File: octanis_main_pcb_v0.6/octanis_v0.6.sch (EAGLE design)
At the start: 103 parts, among them IC1 BME280, IC2 BNO055A, Q1 32.768kHz, Q2 32.768kHz, U1 TPS61232, U10 INA210, U11 INA210, U12 INA210, U13 RN2483, U2 DRV8836DSSR, U3 DRV8836DSSR, U4 MSP432, U5 SST25VF064C, U6 DRV8836DSSR, U7 DRV8836DSSR, U8 MAX6001SOT-23, U9 INA210

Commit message: finalized changes for v0.6. coax connector missing
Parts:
- added DIGITAL_IO2: (no value), pinhead:PINHD-2X5
- added JP1: (no value), pinhead:PINHD-2X2
- added V_MOT1, V_MOT2: (no value), pinhead-2:PINHD-1X02_2.54-S
- added X1: MC-921, con-coax:MC-921
- ANALOG: device pinhead:PINHD-2X10 -> pinhead:PINHD-2X5
- renumbered DIGITAL_IO to DIGITAL_IO1, M7/M1 to M7/M8
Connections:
- removed net A0: ANALOG.1
- removed net P3.7: DIGITAL_IO1.6, U4.P3.7/PM_UCB2SOMI/PM_UCB2SCL
- removed net P5.6_NC: U4.P5.6/TA2.1/VREF+/VEREF+/C1.7
- new net P10.4: DIGITAL_IO2.6, U4.P10.4/TA3.0/C0.7
- new net P10.5: DIGITAL_IO2.5, U4.P10.5/TA3.1/C0.6
- new net P2.1: DIGITAL_IO2.8, U4.P2.1/PM_UCA1CLK
- new net P2.4: DIGITAL_IO2.2, U4.P2.4/PM_TA0.1
- new net P2.5: DIGITAL_IO2.1, U4.P2.5/PM_TA0.2
- new net P2.6: DIGITAL_IO2.4, U4.P2.6/PM_TA0.3
- new net P2.7: DIGITAL_IO2.3, U4.P2.7/PM_TA0.4
- new net P5.6: DIGITAL_IO1.6, U4.P5.6/TA2.1/VREF+/VEREF+/C1.7
- new net P7.4: DIGITAL_IO2.7, U4.P7.4/PM_TA1.4/C0.5
- new net P7.5: DIGITAL_IO2.10, U4.P7.5/PM_TA1.3/C0.4
- new net P7.6: DIGITAL_IO2.9, U4.P7.6/PM_TA1.2/C0.3
- net +3V3: now also JP1.1
- net +5V: now also JP1.3; no longer VMOT_SEL.3
- net 5VEN: now also U4.P2.0/PM_UCA1STE; no longer U4.P2.1/PM_UCA1CLK
- net A1: now also ANALOG.1; no longer ANALOG.2
- net A2: now also ANALOG.4; no longer ANALOG.3
- net A3: now also ANALOG.3; no longer ANALOG.4
- net A4: now also ANALOG.6; no longer ANALOG.5
- net A5: now also ANALOG.5; no longer ANALOG.6
- net A6: now also ANALOG.8; no longer ANALOG.7
- net A7: now also ANALOG.7; no longer ANALOG.8
- net A8: now also ANALOG.10; no longer ANALOG.9
- net A9: now also ANALOG.9; no longer ANALOG.10
- net AGND: now also ANALOG.2
- net GND: now also JP1.2, JP1.4, V_MOT1.1, V_MOT2.1
- net M1234SLEEP: no longer U4.P2.0/PM_UCA1STE
- net M1IN1: no longer U4.P3.6/PM_UCB2SIMO/PM_UCB2SDA
- net M1IN2: no longer U4.P2.4/PM_TA0.1
- net M2IN1: no longer U4.P2.5/PM_TA0.2
- net M2IN2: no longer U4.P2.6/PM_TA0.3
- net M3IN1: no longer U4.P2.7/PM_TA0.4
- net M3IN2: no longer U4.P10.4/TA3.0/C0.7
- net M4IN1: no longer U4.P10.5/TA3.1/C0.6
- net M4IN2: no longer U4.P7.4/PM_TA1.4/C0.5
- net M5678SLEEP: now also U4.P3.1/PM_UCA2CLK; no longer U4.P3.5/PM_UCB2CLK
- net M5IN1: now also U4.P7.7/PM_TA1.1/C0.2; no longer U4.P7.5/PM_TA1.3/C0.4
- net M5IN2: now also U4.P8.0/UCB3STE/TA1.0/C0.1; no longer U4.P7.6/PM_TA1.2/C0.3
- net M6IN1: now also U4.P3.0/PM_UCA2STE; no longer U4.P8.0/UCB3STE/TA1.0/C0.1
- net M6IN2: now also U4.P8.1/UCB3CLK/TA2.0/C0.0; no longer U4.P7.7/PM_TA1.1/C0.2
- net M7IN1: now also U4.P3.4/PM_UCB2STE; no longer U4.P8.1/UCB3CLK/TA2.0/C0.0
- net M7IN2: now also U4.P3.5/PM_UCB2CLK; no longer U4.P3.0/PM_UCA2STE
- net M8IN1: now also U4.P3.6/PM_UCB2SIMO/PM_UCB2SDA; no longer U4.P3.1/PM_UCA2CLK
- net M8IN2: now also U4.P3.7/PM_UCB2SOMI/PM_UCB2SCL; no longer U4.P3.4/PM_UCB2STE
- net V_MOTOR: now also V_MOT1.2
- net V_MOTOR2: now also V_MOT2.2

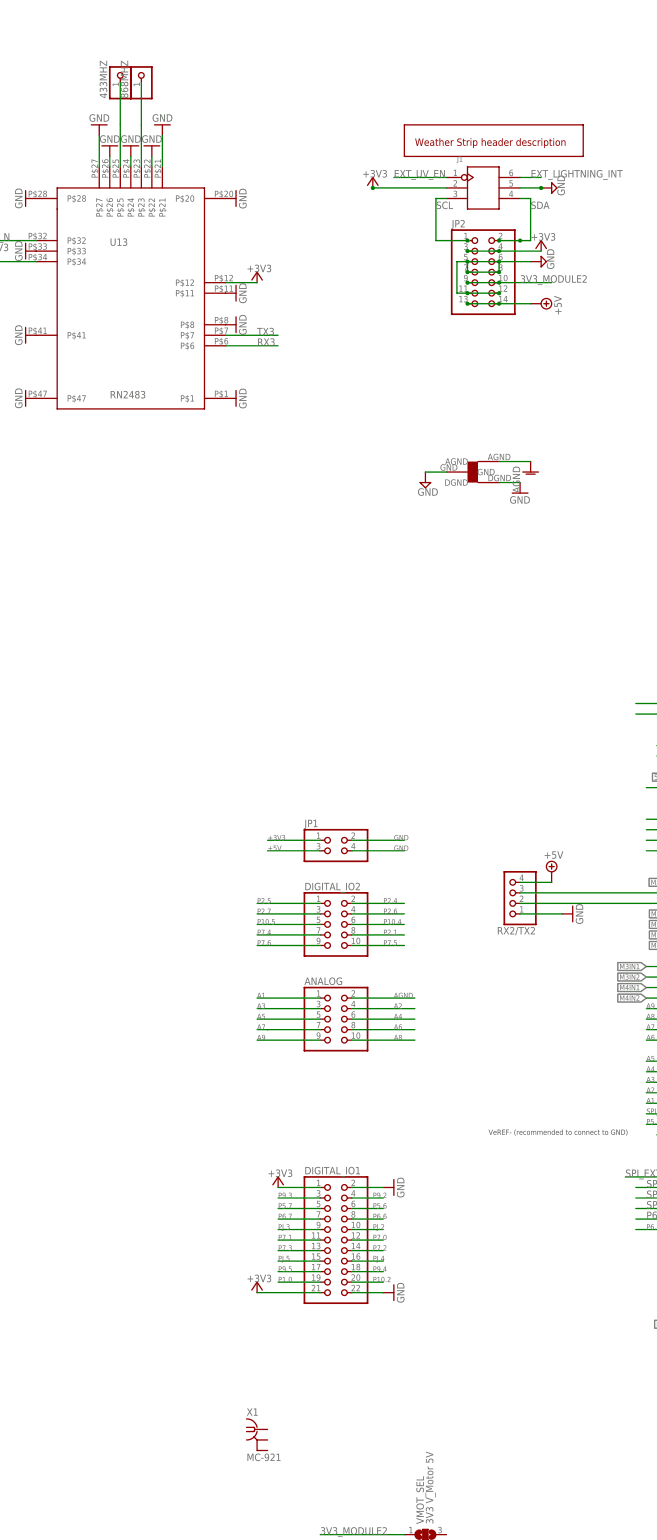
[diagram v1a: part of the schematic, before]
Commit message: added SMA connector for LoRa
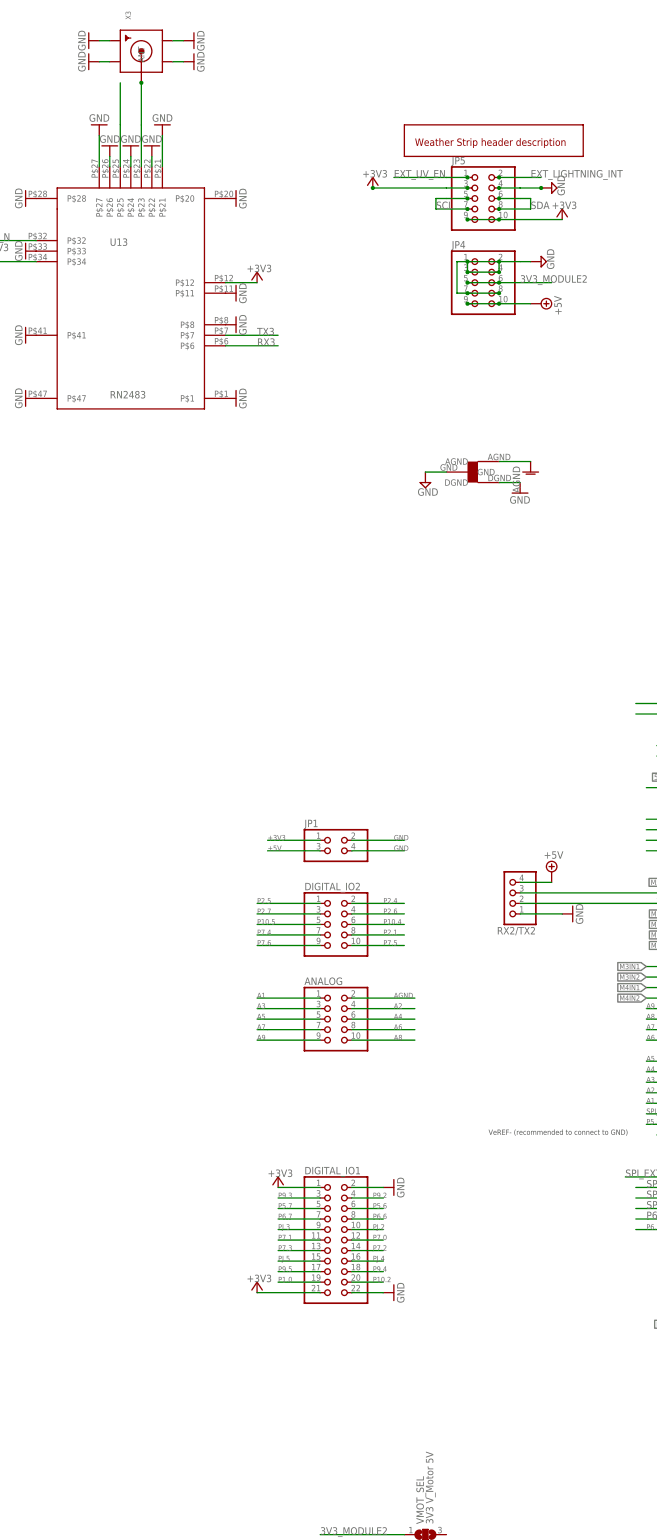
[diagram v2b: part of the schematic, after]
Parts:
- removed 433MHZ, 868MHZ: (no value), Headerlibrary:PINHD-1X1
- removed J1: (no value), Seeed-OPL-Connector:SMD-BLUE-FEMALE-HEADER-VERT(2X3P-2.54)
- removed JP2: (no value), pinhead:PINHD-2X7
- removed X1: MC-921, con-coax:MC-921
- added JP4: (no value), pinhead-2:PINHD-2X05_2.54
- added JP5: (no value), pinhead-2:PINHD-2X05_2.54-SMD
- added X3: (no value), sma_end_launch:SMACONNECTOR_EDGE
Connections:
- net +3V3: now also JP5.10, JP5.3, JP5.9; no longer J1.2, JP2.3, JP2.4
- net +5V: now also JP4.10, JP4.9; no longer JP2.13, JP2.14
- net 3V3_MODULE2: now also JP4.5, JP4.6; no longer JP2.10, JP2.9
- net ANT433: no longer 433MHZ.1
- net ANT868: now also X3.ANT; no longer 868MHZ.1
- net EXT_LIGHTNING_INT: now also JP5.2; no longer J1.6
- net EXT_UV_EN: now also JP5.1; no longer J1.1
- net GND: now also JP4.1, JP4.2, JP4.3, JP4.4, JP4.7, JP4.8, JP5.4, X3.GND1, X3.GND2, X3.GND3, X3.GND4; no longer J1.5, JP2.11, JP2.12, JP2.5, JP2.6, JP2.7, JP2.8
- net SCL: now also JP5.5, JP5.7; no longer J1.3, JP2.1
- net SDA: now also JP5.6, JP5.8; no longer J1.4, JP2.2

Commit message: DRC clean layout
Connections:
- new net V_MOTOR_ALT: VMOT_SEL.3, V_MOT1.2
- net V_MOTOR: no longer V_MOT1.2
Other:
- moved on the sheet: V_MOT1
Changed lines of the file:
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@@
 <instance part="JP1" gate="A" x="193.04" y="297.18"/>
 <instance part="V_MOT2" gate="A" x="563.88" y="142.24"/>
-<instance part="V_MOT1" gate="A" x="314.96" y="129.54"/>
+<instance part="V_MOT1" gate="A" x="236.22" y="132.08"/>
 <instance part="X3" gate="G$1" x="144.78" y="490.22" rot="R90"/>
 <instance part="JP4" gate="A" x="226.06" y="434.34"/>
@@
 <segment>
 <pinref part="V_MOT1" gate="A" pin="1"/>
-<wire x1="312.42" y1="132.08" x2="299.72" y2="132.08" width="0.1524" layer="91"/>
-<label x="299.72" y="132.08" size="1.27" layer="95"/>
+<wire x1="233.68" y1="134.62" x2="220.98" y2="134.62" width="0.1524" layer="91"/>
+<label x="220.98" y="134.62" size="1.27" layer="95"/>
 </segment>
 <segment>
@@
 <label x="327.66" y="109.22" size="1.778" layer="95"/>
 </segment>
-<segment>
-<pinref part="V_MOT1" gate="A" pin="2"/>
-<wire x1="312.42" y1="129.54" x2="299.72" y2="129.54" width="0.1524" layer="91"/>
-<label x="299.72" y="129.54" size="1.27" layer="95"/>
-</segment>
 </net>
 <net name="N$2" class="0">
@@
 </segment>
 </net>
+<net name="V_MOTOR_ALT" class="3">
+<segment>
+<pinref part="V_MOT1" gate="A" pin="2"/>
+<wire x1="233.68" y1="132.08" x2="220.98" y2="132.08" width="0.1524" layer="91"/>
+<label x="220.98" y="132.08" size="1.27" layer="95"/>
+<pinref part="VMOT_SEL" gate="G$1" pin="3"/>
+<wire x1="220.98" y1="132.08" x2="218.44" y2="132.08" width="0.1524" layer="91"/>
+</segment>
+</net>

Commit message: revised silklayer
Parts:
- removed C35, C36: 10n, rcl:C-EUC0603
- removed JP4: (no value), pinhead-2:PINHD-2X05_2.54
- removed R20: 6.8k, rcl:R-EU_R0603
- removed R21: 100k, rcl:R-EU_R0603
- added C3: 100n, rcl:C-EUC0603
- added C8: 22uF, rcl:C-EUC0603
- added JP3: (no value), pinhead:PINHD-2X2
- added R17: 6.8k, rcl:R-EU_R0603
- added R8: 1k, rcl:R-EU_R0603
- C1: value 1n -> 22uF
- C10: value 470n -> 10nF
- C11: value 100n -> 1n
- C12: value 470n -> 10u; device rcl:C-EUC0603 -> rcl:CPOL-EUA/3216-18R
- C13: value 10u -> 100n; device rcl:CPOL-EUA/3216-18R -> rcl:C-EUC0603
- C17: value 12p -> 100n
- C18: value 100n -> 12p; device rcl:C-EUC0603 -> rcl:C-EUC0402
- C19, C20: device rcl:C-EUC0603 -> rcl:C-EUC0402
- C2: value 22uF -> 100n
- C22: value 120n -> 100n
- C23: value 12p -> 470n; device rcl:C-EUC0402 -> rcl:C-EUC0603
- C24: value 100n -> 10n
- C25: value 12p -> 10n; device rcl:C-EUC0402 -> rcl:C-EUC0603
- C26: value 100n -> 470n; device rcl:C-EUC0402 -> rcl:C-EUC0603
- C27, C30: value 470n -> 10n
- C33, C34: value 10n -> 470n
- C4: value 22uF -> 120n
- C5: value 10nF -> 12p
- C6: value 100n -> 12p
- IC1: value BME280 -> BNO055A; device bosch-bme280:BME280 -> BNO055:BNO055A
- IC2: value BNO055A -> BME280; device BNO055:BNO055A -> bosch-bme280:BME280
- JP1: device pinhead:PINHD-2X2 -> pinhead-2:PINHD-2X05_2.54
- LED1: value LED0 -> LED1
- LED2: value LED1 -> LED0
- R1: value 4.7k -> 1M
- R10: value 47k -> 1k
- R11: value 0R -> 1k; device rcl:R-EU_R0402 -> rcl:R-EU_R0603
- R13: value 100k -> 0R; device rcl:R-EU_R0603 -> rcl:R-EU_R0402
- R18: value 6.8k -> 10k
- R19: value 10k -> 6.8k
- R2: value 1k -> 4.7k
- R4, R5: value 1M -> 100k
- R7: value 1k -> 1M
- R9: value 1k -> 47k
- U11, U12: value INA210 -> DRV8836DSSR; device Octanis1_EPS:INA213 -> DRV8834:DRV8836DSSR
- U2: value DRV8836DSSR -> MSP432; device DRV8834:DRV8836DSSR -> MSP-EXP432:MSP432
- U3: value DRV8836DSSR -> MAX6001SOT-23; device DRV8834:DRV8836DSSR -> Octanis1:MAX6001SOT-23
- U4: value MSP432 -> DRV8836DSSR; device MSP-EXP432:MSP432 -> DRV8834:DRV8836DSSR
- U5: value SST25VF064C -> DRV8836DSSR; device BertaLib:SST25VF064C -> DRV8834:DRV8836DSSR
- U6: value DRV8836DSSR -> SST25VF064C; device DRV8834:DRV8836DSSR -> BertaLib:SST25VF064C
- U7: value DRV8836DSSR -> INA210; device DRV8834:DRV8836DSSR -> Octanis1_EPS:INA213
- U8: value MAX6001SOT-23 -> INA210; device Octanis1:MAX6001SOT-23 -> Octanis1_EPS:INA213
- renumbered JP5 to JP2, M5/M1 to M5/M6, U$100 to U$2, U13 to U100, VMOT_SEL2 to VMOT_SEL100, X3 to 868MHZ
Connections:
- net +3V3: now also C12.+, C13.2, C17.1, C21.2, C3.1, C4.1, IC2.CSB, JP3.1, R12.2, R18.2, R2.2, R4.1, R5.2, R9.1, U2.DVCC1, U2.DVCC2, U6.HOLD, U6.VCC, U6.WP; no longer C11.2, C13.+, C20.2, C21.1, C24.1, C6.1, IC1.CSB, JP1.1, R1.2, R10.1, R11.2, R12.1, R19.2, R21.2, U4.DVCC1, U4.DVCC2, U5.HOLD, U5.VCC, U5.WP
- net +5V: now also C8.1, JP1.10, JP1.9, JP3.3, R7.2; no longer C4.1, JP1.3, JP4.10, JP4.9, R5.2
- net 3V3_MODULE2: now also C1.1, JP1.5, JP1.6, R1.2; no longer C2.1, JP4.5, JP4.6, R4.2
- net 5VEN: now also R1.1, U2.P2.0/PM_UCA1STE; no longer R4.1, U4.P2.0/PM_UCA1STE
- net A1: now also U2.P5.4/A1; no longer U4.P5.4/A1
- net A2: now also U2.P5.3/A2; no longer U4.P5.3/A2
- net A20: now also R19.1, U2.P8.5/A20; no longer R20.1, U4.P8.5/A20
- net A20UNF: now also R19.2, U10.OUT; no longer R20.2, U9.OUT
- net A21: now also C31.2, R17.1, U2.P8.4/A21; no longer C28.2, R18.1, U4.P8.4/A21
- net A21UNF: now also R17.2, U9.OUT; no longer R18.2, U10.OUT
- net A22: now also C28.2, U2.P8.3/TA3CLK/A22; no longer C29.2, U4.P8.3/TA3CLK/A22
- net A22UNF: now also U8.OUT; no longer U11.OUT
- net A23: now also C29.2, U2.P8.2/TA3.2/A23; no longer C27.2, U4.P8.2/TA3.2/A23
- net A23UNF: now also U7.OUT; no longer U12.OUT
- net A3: now also U2.P5.2/A3; no longer U4.P5.2/A3
- net A4: now also U2.P5.1/A4; no longer U4.P5.1/A4
- net A5: now also U2.P5.0/A5; no longer U4.P5.0/A5
- net A6: now also U2.P4.7/A6; no longer U4.P4.7/A6
- net A7: now also U2.P4.6/A7; no longer U4.P4.6/A7
- net A8: now also U2.P4.5/A8; no longer U4.P4.5/A8
- net A9: now also U2.P4.4/HSMCLK/SVMHOUT/A9; no longer U4.P4.4/HSMCLK/SVMHOUT/A9
- net ACCEL_INT: now also IC1.INT, U2.P1.1/UCA0CLK; no longer IC2.INT, U4.P1.1/UCA0CLK
- net ACCEL_N_BOOTLD: now also IC1.BOOT_LOAD_PIN, R5.1; no longer IC2.BOOT_LOAD_PIN, R13.1
- net ACCEL_N_RST: now also IC1.RESET, R4.2, U2.P10.3UCB3SOMI/UCB3SCL; no longer IC2.RESET, R12.2, U4.P10.3UCB3SOMI/UCB3SCL
- net AGND: now also C20.2, C24.1, C25.1, C30.1, C31.1, U2.AVSS1, U2.AVSS2, U2.AVSS3, U3.GND, U7.GND; no longer C26.2, C33.1, C34.1, C35.1, C36.1, U11.GND, U12.GND, U4.AVSS1, U4.AVSS2, U4.AVSS3
- net AVCC: now also C20.1, R13.1, U2.AVCC1, U2.AVCC2; no longer C26.1, R11.1, U4.AVCC1, U4.AVCC2
- net CURR_SENSE_EN: now also C24.2, C25.2, C27.2, C30.2, U2.P8.6/A19, U3.IN, U7.VCC, U8.VCC; no longer C33.2, C34.2, C35.2, C36.2, U11.VCC, U12.VCC, U4.P8.6/A19, U8.IN
- net EXT_LIGHTNING_INT: now also U2.P1.4/UCB0STE; no longer U4.P1.4/UCB0STE
- net EXT_UV_EN: now also U2.P1.5/UCB0CLK; no longer U4.P1.5/UCB0CLK
- net GND: now also C1.2, C10.2, C12.-, C13.1, C19.1, C2.1, C21.1, C26.1, C3.2, C33.1, C34.1, C8.2, IC1.COM2, IC1.COM3, IC1.GNDIO, IC1.PIN10, IC1.PIN15, IC1.PIN16, IC1.PS0, IC1.PS1, IC2.SDO, JP1.1, JP1.3, JP1.7, JP1.8, JP3.2, JP3.4, R10.1, R11.1, U11.EPAD, U11.GND, U12.EPAD, U12.GND, U2.DVSS1, U2.DVSS2, U2.DVSS3, U4.EPAD, U4.GND, U5.EPAD; no longer C1.1, C10.1, C12.1, C13.-, C19.2, C2.2, C20.1, C21.2, C24.2, C25.1, C30.1, C31.1, IC1.SDO, IC2.COM2, IC2.COM3, IC2.GNDIO, IC2.PIN10, IC2.PIN15, IC2.PIN16, IC2.PS0, IC2.PS1, JP4.1, JP4.2, JP4.3, JP4.4, JP4.7, JP4.8, R6.1, R7.1, U2.EPAD, U2.GND, U3.EPAD, U3.GND, U4.DVSS1, U4.DVSS2, U4.DVSS3, U6.EPAD, U7.EPAD, U7.GND
- net LED0: now also LED2.A, U2.P10.0/UCB3STE; no longer LED1.A, U4.P10.0/UCB3STE
- net LED1: now also LED1.A, U2.P10.1/UCB3CLK; no longer LED2.A, U4.P10.1/UCB3CLK
- net LORA_RST_N: now also R12.1; no longer R21.1
- net M1234SLEEP: now also U11.MODE, U11.NSLEEP, U12.MODE, U12.NSLEEP, U2.P8.7/A18; no longer U2.MODE, U2.NSLEEP, U3.MODE, U3.NSLEEP, U4.P8.7/A18
- net M1IN1: now also U11.AIN1_/_APHASE, U2.P9.0/A17; no longer U2.AIN1_/_APHASE, U4.P9.0/A17
- net M1IN2: now also U11.AIN2_/_AENBL, U2.P9.1/A16; no longer U2.AIN2_/_AENBL, U4.P9.1/A16
- net M2IN1: now also U11.BIN1_/_BPHASE, U2.P6.0/A15; no longer U2.BIN1_/_BPHASE, U4.P6.0/A15
- net M2IN2: now also U11.BIN2_/_BENBL, U2.P6.1/A14; no longer U2.BIN2_/_BENBL, U4.P6.1/A14
- net M3IN1: now also U12.AIN1_/_APHASE, U2.P4.0/A13; no longer U3.AIN1_/_APHASE, U4.P4.0/A13
- net M3IN2: now also U12.AIN2_/_AENBL, U2.P4.1/A12; no longer U3.AIN2_/_AENBL, U4.P4.1/A12
- net M4IN1: now also U12.BIN1_/_BPHASE, U2.P4.2/ACLK/TA2CLK/A11; no longer U3.BIN1_/_BPHASE, U4.P4.2/ACLK/TA2CLK/A11
- net M4IN2: now also U12.BIN2_/_BENBL, U2.P4.3/MCLK/RTCCLK/A10; no longer U3.BIN2_/_BENBL, U4.P4.3/MCLK/RTCCLK/A10
- net M5678SLEEP: now also U2.P3.1/PM_UCA2CLK, U4.MODE, U4.NSLEEP, U5.MODE, U5.NSLEEP; no longer U4.P3.1/PM_UCA2CLK, U6.MODE, U6.NSLEEP, U7.MODE, U7.NSLEEP
- net M5IN1: now also U2.P7.7/PM_TA1.1/C0.2, U4.AIN1_/_APHASE; no longer U4.P7.7/PM_TA1.1/C0.2, U7.AIN1_/_APHASE
- net M5IN2: now also U2.P8.0/UCB3STE/TA1.0/C0.1, U4.AIN2_/_AENBL; no longer U4.P8.0/UCB3STE/TA1.0/C0.1, U7.AIN2_/_AENBL
- net M5OUT1: now also RS1.I1, U4.AOUT1; no longer RS4.I1, U7.AOUT1
- net M6IN1: now also U2.P3.0/PM_UCA2STE, U4.BIN1_/_BPHASE; no longer U4.P3.0/PM_UCA2STE, U7.BIN1_/_BPHASE
- net M6IN2: now also U2.P8.1/UCB3CLK/TA2.0/C0.0, U4.BIN2_/_BENBL; no longer U4.P8.1/UCB3CLK/TA2.0/C0.0, U7.BIN2_/_BENBL
- net M7IN1: now also U2.P3.4/PM_UCB2STE, U5.AIN1_/_APHASE; no longer U4.P3.4/PM_UCB2STE, U6.AIN1_/_APHASE
- net M7IN2: now also U2.P3.5/PM_UCB2CLK, U5.AIN2_/_AENBL; no longer U4.P3.5/PM_UCB2CLK, U6.AIN2_/_AENBL
- net M8IN1: now also U2.P3.6/PM_UCB2SIMO/PM_UCB2SDA, U5.BIN1_/_BPHASE; no longer U4.P3.6/PM_UCB2SIMO/PM_UCB2SDA, U6.BIN1_/_BPHASE
- net M8IN2: now also U2.P3.7/PM_UCB2SOMI/PM_UCB2SCL, U5.BIN2_/_BENBL; no longer U4.P3.7/PM_UCB2SOMI/PM_UCB2SCL, U6.BIN2_/_BENBL
- net N$1: now also U2.VCORE; no longer U4.VCORE
- net N$10: now also C19.2, U2.PJ.1/LFXOUT; no longer C25.2, U4.PJ.1/LFXOUT
- net N$13: now also U12.AOUT1; no longer U3.AOUT1
- net N$14: now also R6.1; no longer R2.1
- net N$15: now also RS1.V2, U7.IN-; no longer RS4.V2, U12.IN-
- net N$17: now also RS1.V1, U7.IN+; no longer RS4.V1, U12.IN+
- net N$18: now also C2.2, IC1.CAP; no longer C18.2, IC2.CAP
- net N$19: now also C5.1, IC1.XIN32; no longer C19.1, IC2.XIN32
- net N$2: now also R7.1; no longer R5.1
- net N$21: now also RS1.I2; no longer RS4.I2
- net N$23: now also RS2.V1, U8.IN+; no longer RS3.V1, U11.IN+
- net N$24: now also RS2.V2, U8.IN-; no longer RS3.V2, U11.IN-
- net N$25: now also RS2.I1, U4.BOUT1; no longer RS3.I1, U7.BOUT1
- net N$26: now also R8.1; no longer R9.1
- net N$27: now also RS2.I2; no longer RS3.I2
- net N$28: now also RS3.V2, U9.IN-; no longer RS2.V2, U10.IN-
- net N$29: now also RS3.V1, U9.IN+; no longer RS2.V1, U10.IN+
- net N$30: now also RS4.V2, U10.IN-; no longer RS1.V2, U9.IN-
- net N$31: now also RS4.V1, U10.IN+; no longer RS1.V1, U9.IN+
- net N$32: now also RS3.I2; no longer RS2.I2
- net N$33: now also U2.DCOR; no longer U4.DCOR
- net N$34: now also U2.VSW; no longer U4.VSW
- net N$35: now also RS4.I1, U5.BOUT1; no longer RS1.I1, U6.BOUT1
- net N$36: now also RS3.I1, U5.AOUT1; no longer RS2.I1, U6.AOUT1
- net N$37: now also RS4.I2; no longer RS1.I2
- net N$38: now also U4.AOUT2; no longer U7.AOUT2
- net N$39: now also U12.AOUT2; no longer U3.AOUT2
- net N$4: now also R8.2; no longer R9.2
- net N$40: now also U12.BOUT1; no longer U3.BOUT1
- net N$41: now also U12.BOUT2; no longer U3.BOUT2
- net N$42: now also C10.1; no longer C5.1
- net N$43: now also U4.BOUT2; no longer U7.BOUT2
- net N$44: now also R6.2; no longer R2.2
- net N$45: now also U5.BOUT2; no longer U6.BOUT2
- net N$49: now also U11.AOUT1; no longer U2.AOUT1
- net N$5: now also LED2.C, R11.2; no longer LED1.C, R7.2
- net N$50: now also U11.AOUT2; no longer U2.AOUT2
- net N$51: now also U11.BOUT1; no longer U2.BOUT1
- net N$52: now also U11.BOUT2; no longer U2.BOUT2
- net N$54: now also U5.AOUT2; no longer U6.AOUT2
- net N$6: now also LED1.C, R10.2; no longer LED2.C, R6.2
- net N$73: now also C6.1, IC1.XOUT32; no longer C17.1, IC2.XOUT32
- net N$76: now also U2.SWDIOTMS; no longer U4.SWDIOTMS
- net N$77: now also U2.SWCLKTCK; no longer U4.SWCLKTCK
- net N$8: now also C18.2, U2.PJ.0/LFXIN; no longer C23.2, U4.PJ.0/LFXIN
- net P1.0: now also U2.P1.0/UCA0STE; no longer U4.P1.0/UCA0STE
- net P10.2: now also U2.P10.2/UCB3SIMO/UCB3SDA; no longer U4.P10.2/UCB3SIMO/UCB3SDA
- net P10.4: now also U2.P10.4/TA3.0/C0.7; no longer U4.P10.4/TA3.0/C0.7
- net P10.5: now also U2.P10.5/TA3.1/C0.6; no longer U4.P10.5/TA3.1/C0.6
- net P2.1: now also U2.P2.1/PM_UCA1CLK; no longer U4.P2.1/PM_UCA1CLK
- net P2.4: now also U2.P2.4/PM_TA0.1; no longer U4.P2.4/PM_TA0.1
- net P2.5: now also U2.P2.5/PM_TA0.2; no longer U4.P2.5/PM_TA0.2
- net P2.6: now also U2.P2.6/PM_TA0.3; no longer U4.P2.6/PM_TA0.3
- net P2.7: now also U2.P2.7/PM_TA0.4; no longer U4.P2.7/PM_TA0.4
- net P5.6: now also U2.P5.6/TA2.1/VREF+/VEREF+/C1.7; no longer U4.P5.6/TA2.1/VREF+/VEREF+/C1.7
- net P5.7: now also U2.P5.7/TA2.2/VREF-/VEREF-/C1.6; no longer U4.P5.7/TA2.2/VREF-/VEREF-/C1.6
- net P6.6: now also U2.P6.6/TA2.3/UCB3SIMO/UCB3SDA/C1.1; no longer U4.P6.6/TA2.3/UCB3SIMO/UCB3SDA/C1.1
- net P6.7: now also U2.P6.7/TA2.4/UCB3SOMI/UCB3SCL/C1.0; no longer U4.P6.7/TA2.4/UCB3SOMI/UCB3SCL/C1.0
- net P7.0: now also U2.P7.0/PM_SMCLK/PM_DMAE0; no longer U4.P7.0/PM_SMCLK/PM_DMAE0
- net P7.1: now also U2.P7.1/PM_C0OUT/PM_TA0CLK; no longer U4.P7.1/PM_C0OUT/PM_TA0CLK
- net P7.2: now also U2.P7.2/PM_C1OUT/PM_TA1CLK; no longer U4.P7.2/PM_C1OUT/PM_TA1CLK
- net P7.3: now also U2.P7.3/PM_TA0.0; no longer U4.P7.3/PM_TA0.0
- net P7.4: now also U2.P7.4/PM_TA1.4/C0.5; no longer U4.P7.4/PM_TA1.4/C0.5
- net P7.5: now also U2.P7.5/PM_TA1.3/C0.4; no longer U4.P7.5/PM_TA1.3/C0.4
- net P7.6: now also U2.P7.6/PM_TA1.2/C0.3; no longer U4.P7.6/PM_TA1.2/C0.3
- net P9.2: now also U2.P9.2/TA3.3; no longer U4.P9.2/TA3.3
- net P9.3: now also U2.P9.3/TA3.4; no longer U4.P9.3/TA3.4
- net P9.4: now also U2.P9.4/UCA3STE; no longer U4.P9.4/UCA3STE
- net P9.5: now also U2.P9.5/UCA3CLK; no longer U4.P9.5/UCA3CLK
- net PJ.2: now also U2.PJ.2/HFXOUT; no longer U4.PJ.2/HFXOUT
- net PJ.3: now also U2.PJ.3/HFXIN; no longer U4.PJ.3/HFXIN
- net PJ.4: now also U2.PJ.4/TDI/ADC14CLK; no longer U4.PJ.4/TDI/ADC14CLK
- net PJ.5: now also U2.PJ.5/TDO/SWO; no longer U4.PJ.5/TDO/SWO
- net RST_N: now also C11.2, R9.2, U2.RSTN/NMI; no longer C1.2, R10.2, U4.RSTN/NMI
- net RX0: now also U2.P1.2/UCA0RXD/UCA0SOMI; no longer U4.P1.2/UCA0RXD/UCA0SOMI
- net RX1: now also U2.P2.2/PM_UCA1RXD/PM_UCA1SOMI; no longer U4.P2.2/PM_UCA1RXD/PM_UCA1SOMI
- net RX2: now also U2.P3.2/PM_UCA2RXD/PM_UCA2SOMI; no longer U4.P3.2/PM_UCA2RXD/PM_UCA2SOMI
- net RX3: now also U2.P9.6/UCA3RXD/UCA3SOMI; no longer U4.P9.6/UCA3RXD/UCA3SOMI
- net SCL: now also IC1.COM1, IC2.SCK, R2.1, U2.P1.7/UCB0SOMI/UCB0SCL; no longer IC1.SCK, IC2.COM1, R1.1, U4.P1.7/UCB0SOMI/UCB0SCL
- net SDA: now also IC1.COM0, IC2.SDI, U2.P1.6/UCB0SIMO/UCB0SDA; no longer IC1.SDI, IC2.COM0, U4.P1.6/UCB0SIMO/UCB0SDA
- net SPI_EXTSLAVE_TE: now also U2.P6.2/UCB1STE/C1.5; no longer U4.P6.2/UCB1STE/C1.5
- net SPI_FLASH_CS: now also R18.1, U2.P5.5/A0, U6.CS; no longer R19.1, U4.P5.5/A0, U5.CS
- net SPI_MISO: now also U2.P6.5/UCB1SOMI/UCB1SCL/C1.2, U6.MISO; no longer U4.P6.5/UCB1SOMI/UCB1SCL/C1.2, U5.MISO
- net SPI_MOSI: now also U2.P6.4/UCB1SIMO/UCB1SDA/C1.3, U6.MOSI; no longer U4.P6.4/UCB1SIMO/UCB1SDA/C1.3, U5.MOSI
- net SPI_SCK: now also U2.P6.3/UCB1CLK/C1.4, U6.SCK; no longer U4.P6.3/UCB1CLK/C1.4, U5.SCK
- net TX0: now also U2.P1.3/UCA0TXD/UCA0SIMO; no longer U4.P1.3/UCA0TXD/UCA0SIMO
- net TX1: now also U2.P2.3/PM_UCA1TXD/PM_UCA1SIMO; no longer U4.P2.3/PM_UCA1TXD/PM_UCA1SIMO
- net TX2: now also U2.P3.3/PM_UCA2TXD/PM_UCA2SIMO; no longer U4.P3.3/PM_UCA2TXD/PM_UCA2SIMO
- net TX3: now also U2.P9.7/UCA3TXD/UCA3SIMO; no longer U4.P9.7/UCA3TXD/UCA3SIMO
- net VREF_M: now also U3.OUT, U7.REF, U8.REF; no longer U11.REF, U12.REF, U8.OUT
- net V_MOTOR: now also C33.2, C34.2, U11.VCC, U12.VCC; no longer C10.2, C12.2, U2.VCC, U3.VCC
- net V_MOTOR2: now also C23.2, C26.2, U4.VCC, U5.VCC, V_MOT1.2; no longer C30.2, C31.2, U6.VCC, U7.VCC, V_MOT2.2
- net V_MOTOR_ALT: now also V_MOT2.2; no longer V_MOT1.2
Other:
- moved on the sheet: C1, C10, C11, C17, C18, C19, C2, C20, C21, C22, C23, C24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
